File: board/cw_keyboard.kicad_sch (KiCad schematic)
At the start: 11 parts, among them J1 USB_A, U1 ATtiny44A-P, Y1 20MHz

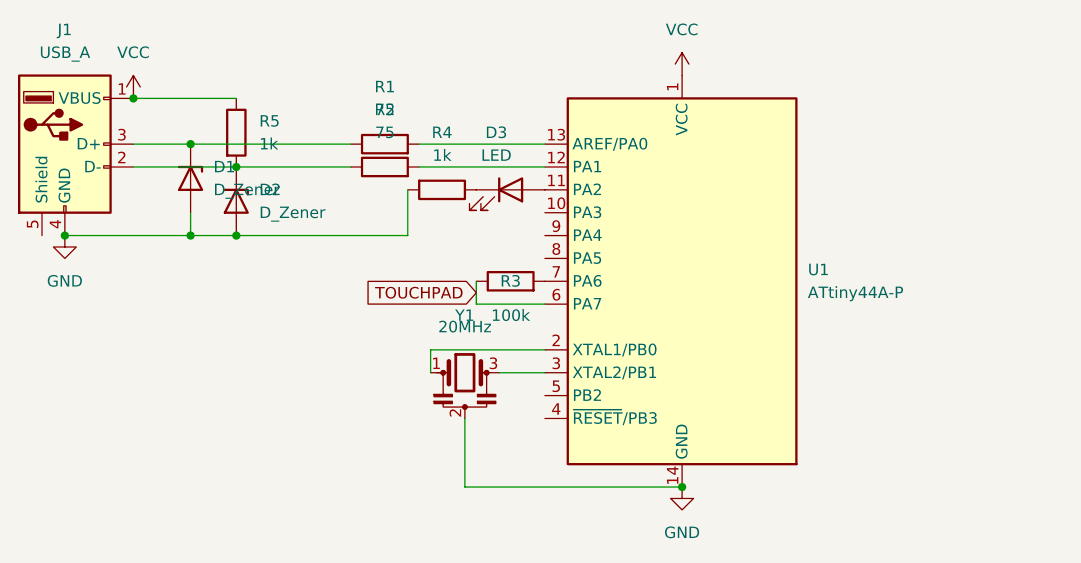
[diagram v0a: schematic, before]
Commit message: feat: add bypass capacitor
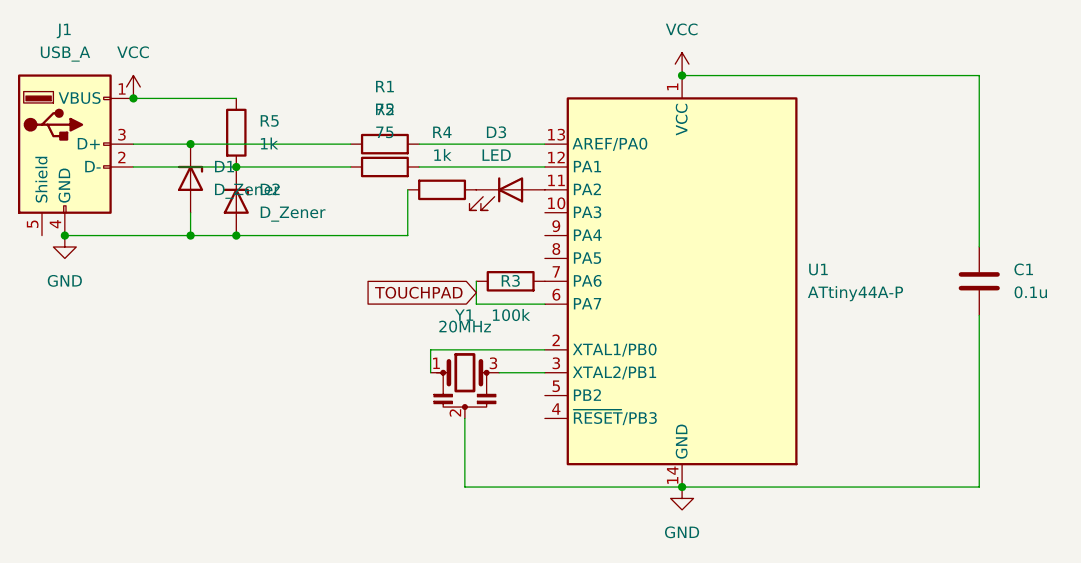
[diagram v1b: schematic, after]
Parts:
- added C1: 0.1u, Capacitor_SMD:C_0603_1608Metric_Pad1.08x0.95mm_HandSolder, symbol Device:C
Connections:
- net GND: now also C1.2
- net VCC: now also C1.1
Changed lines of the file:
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@@
   (junction (at 121.92 78.74) (diameter 0) (color 0 0 0 0)
   )
+  (junction (at 176.53 60.96) (diameter 0) (color 0 0 0 0)
+  )
   (junction (at 121.92 68.58) (diameter 0) (color 0 0 0 0)
   )
@@
     (stroke (width 0) (type default))
   )
+  (wire (pts (xy 209.55 80.01) (xy 209.55 60.96))
+    (stroke (width 0) (type default))
+  )
   (wire (pts (xy 127 71.12) (xy 139.7 71.12))
     (stroke (width 0) (type default))
@@
     (stroke (width 0) (type default))
   )
+  (wire (pts (xy 209.55 87.63) (xy 209.55 106.68))
+    (stroke (width 0) (type default))
+  )
+  (wire (pts (xy 209.55 60.96) (xy 176.53 60.96))
+    (stroke (width 0) (type default))
+  )
   (wire (pts (xy 127 78.74) (xy 146.05 78.74))
     (stroke (width 0) (type default))
   )
   (wire (pts (xy 121.92 68.58) (xy 139.7 68.58))
+    (stroke (width 0) (type default))
+  )
+  (wire (pts (xy 209.55 106.68) (xy 176.53 106.68))
     (stroke (width 0) (type default))
   )
@@
         )
       )
+    )
+  )
+  (symbol (lib_id "Device:C") (at 209.55 83.82 0) (unit 1)
+    (in_bom yes) (on_board yes) (dnp no) (fields_autoplaced)
+    (property "Reference" "C1" (at 213.36 82.55 0)
+      (effects (font (size 1.27 1.27)) (justify left))
+    )
+    (property "Value" "0.1u" (at 213.36 85.09 0)
+      (effects (font (size 1.27 1.27)) (justify left))
+    )
+    (property "Footprint" "Capacitor_SMD:C_0603_1608Metric_Pad1.08x0.95mm_HandSolder" (at 210.5152 87.63 0)
+      (effects (font (size 1.27 1.27)) hide)
+    )
+    (property "Datasheet" "~" (at 209.55 83.82 0)
+      (effects (font (size 1.27 1.27)) hide)
+    )
+    (pin "1")
+    (pin "2")
+    (instances
+      (project "cw_keyboard"
+        (path "/a3eb97fc-52c5-44c0-91a5-9a78099bcb2d"
+          (reference "C1") (unit 1)
+        )
+      )

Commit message: feat: add jumper to switch US/JIS layout
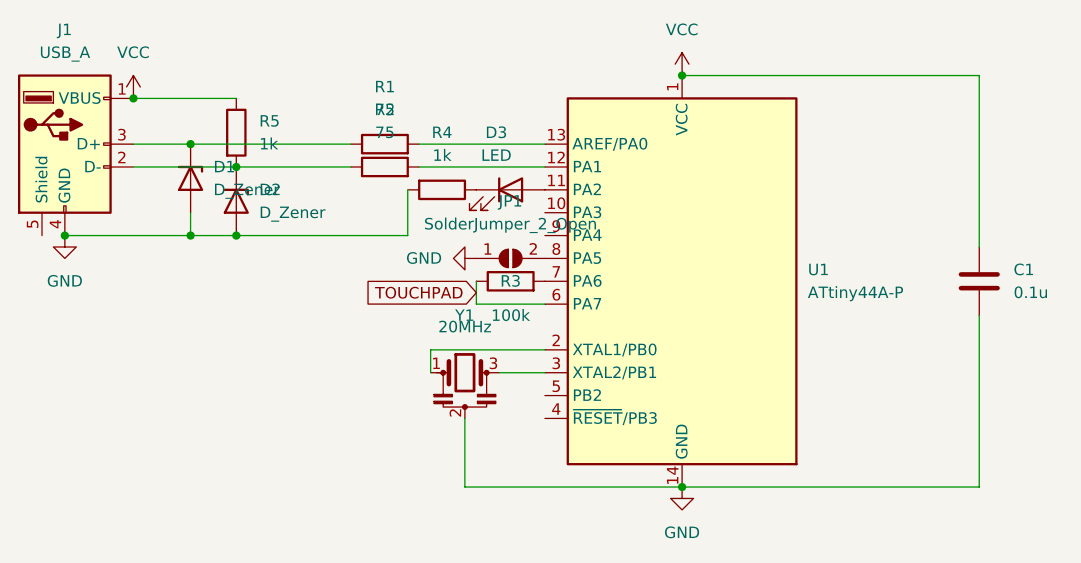
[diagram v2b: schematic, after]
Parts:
- added JP1: SolderJumper_2_Open, Jumper:SolderJumper-2_P1.3mm_Open_RoundedPad1.0x1.5mm, symbol Jumper:SolderJumper_2_Open
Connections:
- net GND: now also JP1.1 (A)
- net at U1.8 (PA5): now also JP1.2 (B)
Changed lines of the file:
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@@
+    )
+  )
+  (symbol (lib_id "Jumper:SolderJumper_2_Open") (at 157.48 81.28 0) (unit 1)
+    (in_bom yes) (on_board yes) (dnp no) (fields_autoplaced)
+    (property "Reference" "JP1" (at 157.48 74.93 0)
+      (effects (font (size 1.27 1.27)))
+    )
+    (property "Value" "SolderJumper_2_Open" (at 157.48 77.47 0)
+      (effects (font (size 1.27 1.27)))
+    )
+    (property "Footprint" "Jumper:SolderJumper-2_P1.3mm_Open_RoundedPad1.0x1.5mm" (at 157.48 81.28 0)
+      (effects (font (size 1.27 1.27)) hide)
+    )
+    (property "Datasheet" "~" (at 157.48 81.28 0)
+      (effects (font (size 1.27 1.27)) hide)
+    )
+    (pin "1")
+    (pin "2")
+    (instances
+      (project "cw_keyboard"
+        (path "/a3eb97fc-52c5-44c0-91a5-9a78099bcb2d"
+          (reference "JP1") (unit 1)
+        )
+      )
     )
   )
@@
         )
       )
+    )
+  )
+  (symbol (lib_id "power:GND") (at 153.67 81.28 270) (unit 1)
+    (in_bom yes) (on_board yes) (dnp no) (fields_autoplaced)
+    (property "Reference" "#PWR05" (at 147.32 81.28 0)
+      (effects (font (size 1.27 1.27)) hide)
+    )
+    (property "Value" "GND" (at 149.86 81.28 90)
+      (effects (font (size 1.27 1.27)) (justify right))
+    )
+    (property "Footprint" "" (at 153.67 81.28 0)
+      (effects (font (size 1.27 1.27)) hide)
+    )
+    (property "Datasheet" "" (at 153.67 81.28 0)
+      (effects (font (size 1.27 1.27)) hide)
+    )
+    (pin "1")
+    (instances
+      (project "cw_keyboard"
+        (path "/a3eb97fc-52c5-44c0-91a5-9a78099bcb2d"
+          (reference "#PWR05") (unit 1)
+        )
+      )
